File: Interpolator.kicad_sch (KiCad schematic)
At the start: 79 parts, among them J1 DA15_Receptacle_MountingHoles, J2 DA15_Receptacle_MountingHoles, J3 Conn_01x12, J4 Conn_01x12, SW1 SW_Push, U1 UA9638C, U2 UA9638C, U3 ICTW8, U5 24AA02-OT, U6 MCP1754S-3302xMB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

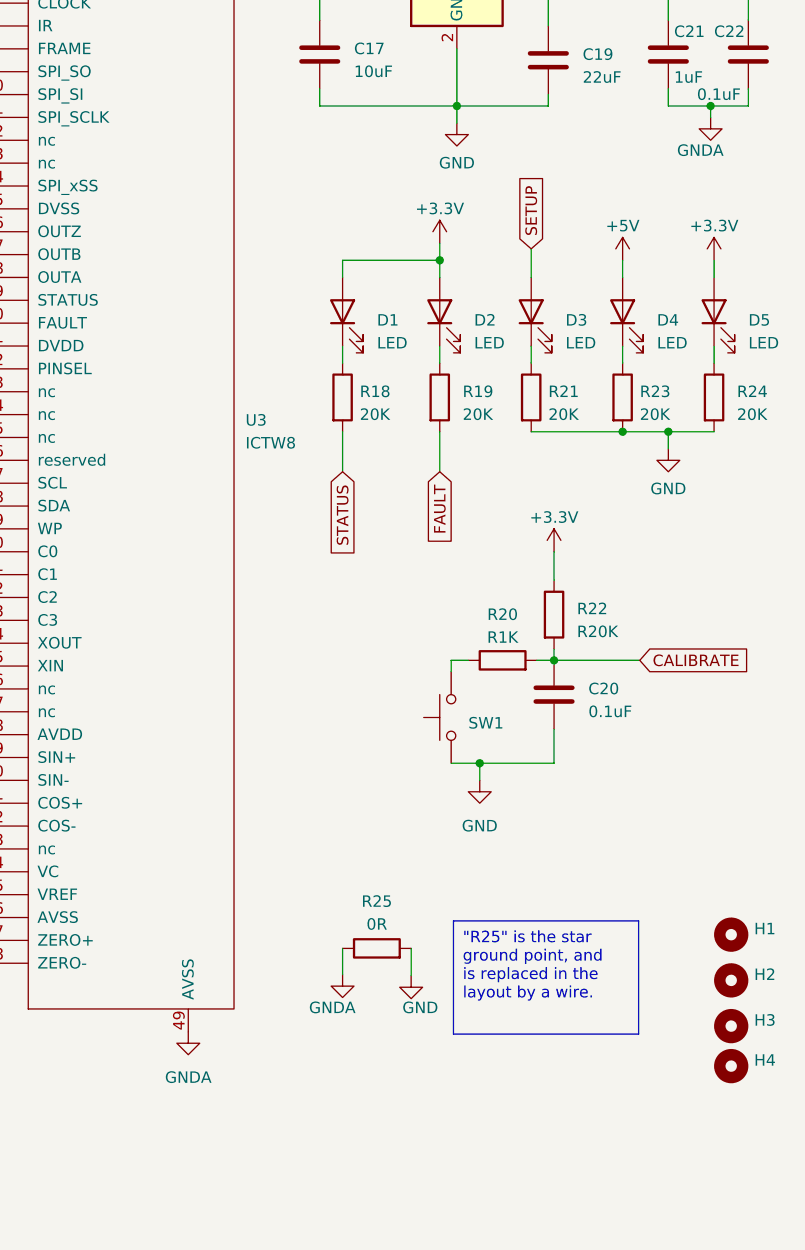
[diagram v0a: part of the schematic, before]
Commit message: Update a few footprints, remove the 5v rail power LED, move all of the LED resistors to one 20K network
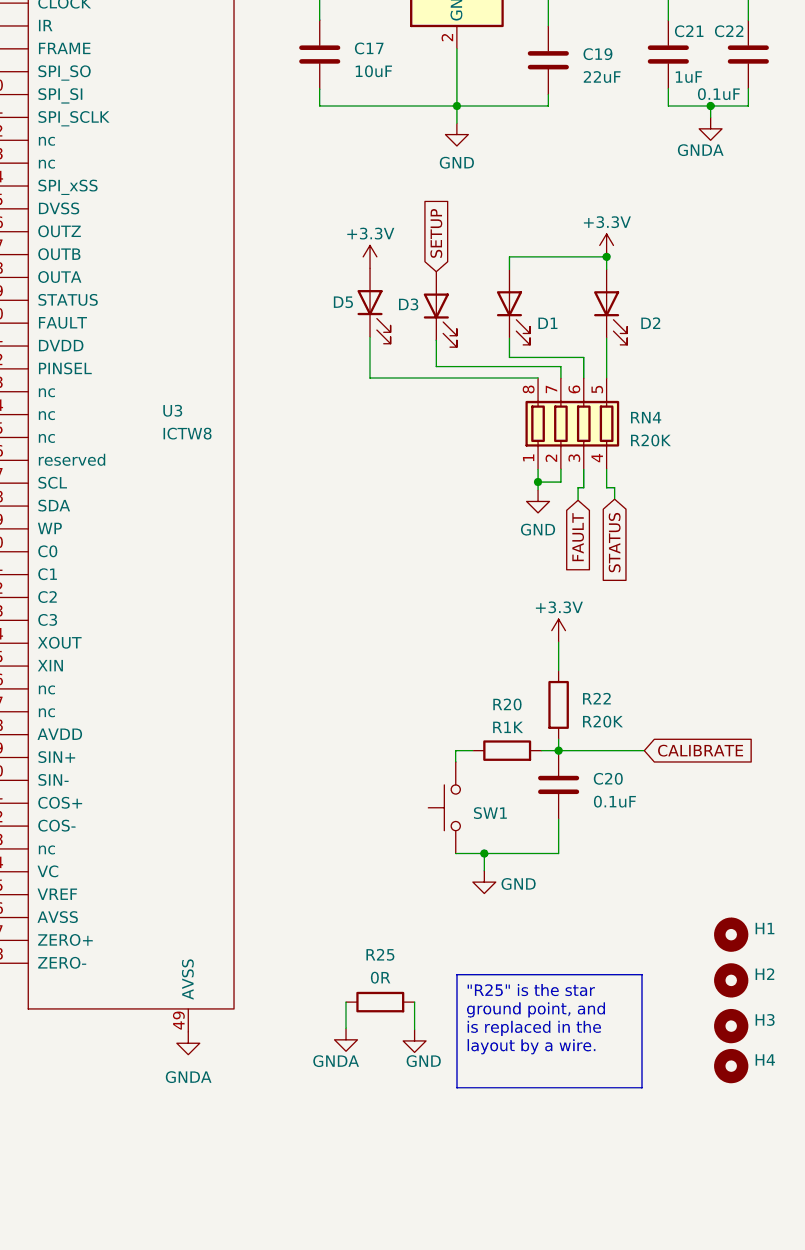
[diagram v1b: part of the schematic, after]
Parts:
- removed D4: LED, encoder-interpolator:LED_0603_1608Metric_Pad1.05x0.95mm_HandSolder, symbol encoder-interpolator:LED
- removed R18, R19, R21, R23, R24: 20K, encoder-interpolator:R_0603_1608Metric, symbol encoder-interpolator:R
- added RN4: R20K, encoder-interpolator:R_Array_Convex_4x0603, symbol encoder-interpolator:R_Pack04
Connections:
- net FAULT: now also RN4.3 (R3.1)
- net GND: now also RN4.1 (R1.1), RN4.2 (R2.1)
- net STATUS: now also RN4.4 (R4.1)
- net at D1.1 (K): now also RN4.6 (R3.2)
- net at D3.1 (K): now also RN4.7 (R2.2)
- net at D5.1 (K): now also RN4.8 (R1.2)
- net at D2.1 (K): now also RN4.5 (R4.2)
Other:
- moved on the sheet: C20, D1, D2, D3, D5, R20, R22, R25, SW1
